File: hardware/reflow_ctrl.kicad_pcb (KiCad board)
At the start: 2 copper layers, 22 parts, among them IC1 MAX6675, U2 MOC3063, U3 BTA41/600B, X1 Master, X2 Mains, X3 Load, X4 Thermocouple

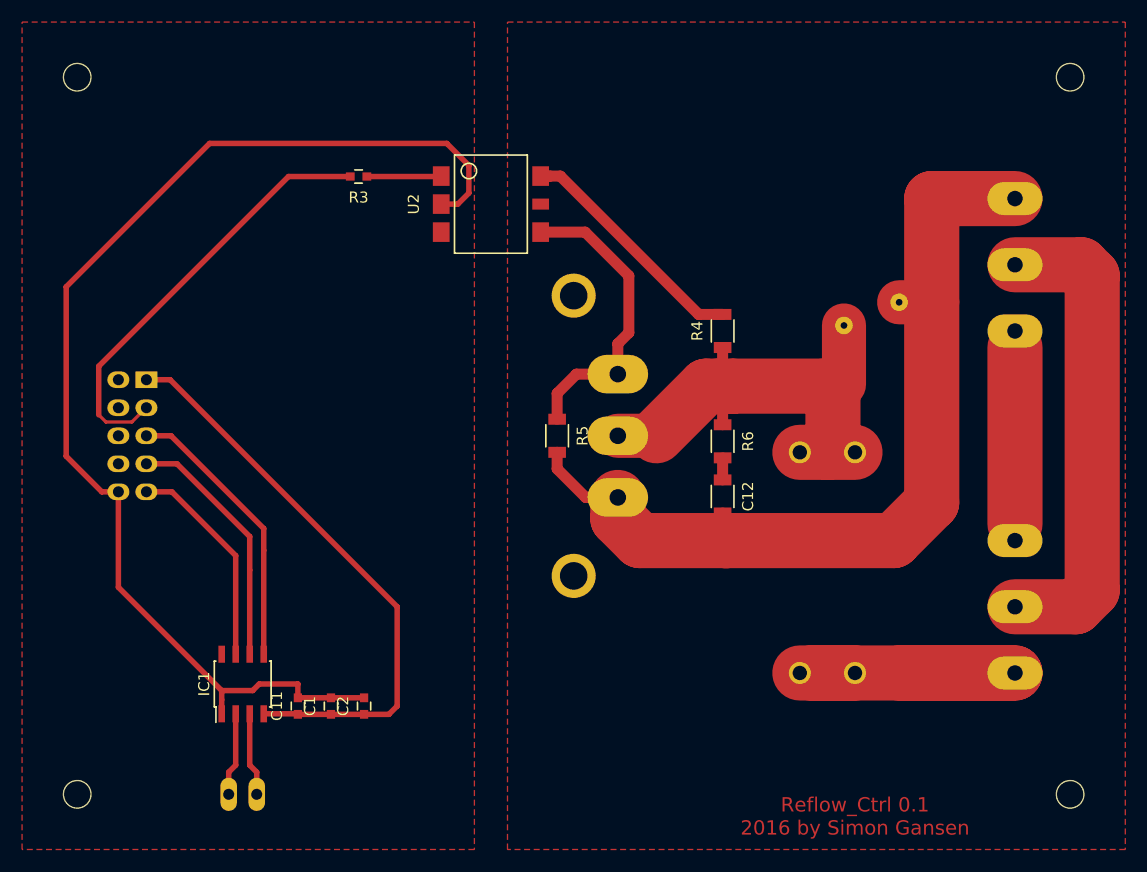
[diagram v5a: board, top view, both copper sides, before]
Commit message: Optimize header pinout and trace widths
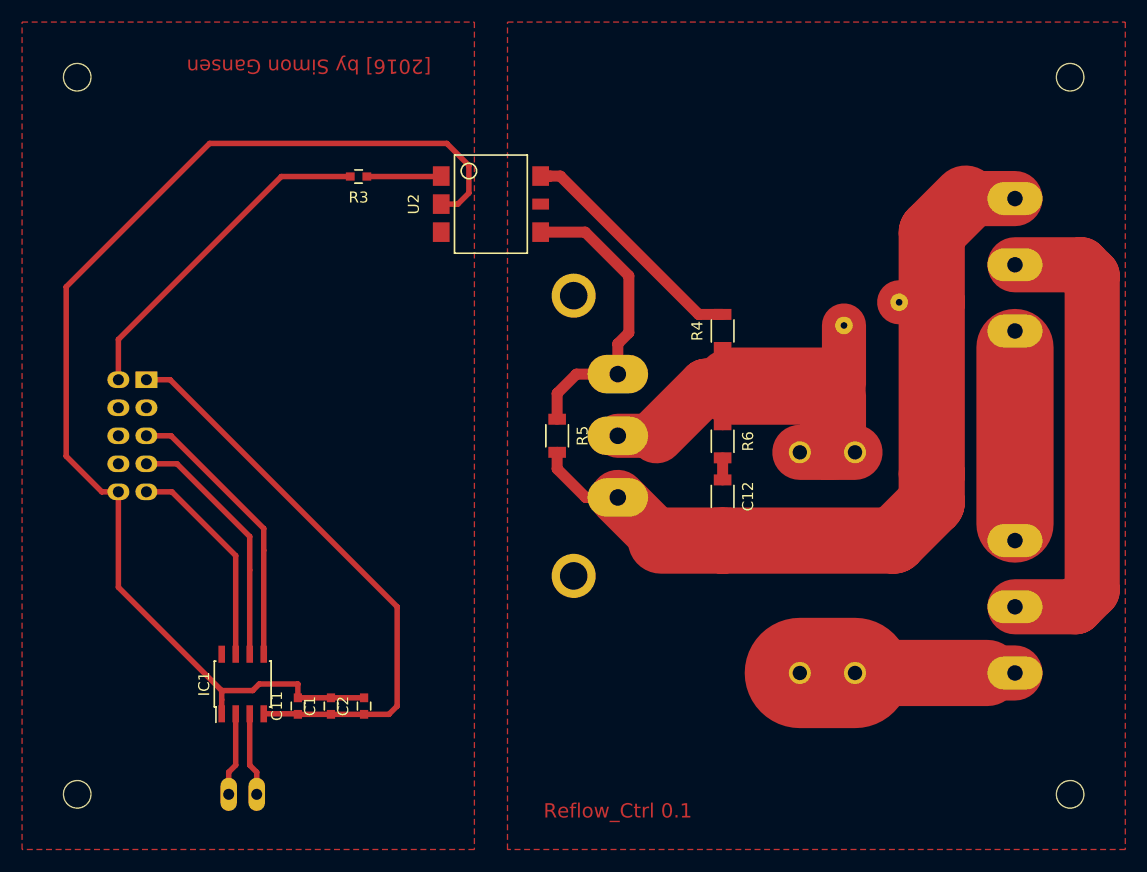
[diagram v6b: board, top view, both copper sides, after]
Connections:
- HS1 pad 1: (no net) -> /PE_mains
- X1 pad 2: (no net) -> /PWR
- X1 pad 3: /PWR -> (no net)
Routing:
- net /L_mains: track 34.0 -> 19.5 mm
- net /PWR: track 39.4 -> 30.8 mm
- net /L_load: track 84.8 -> 81.5 mm
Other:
- rule trace_min: 0.2 -> 0.3
- board text added: "Reflow_Ctrl 0.1"
- board text added: "[2016] by Simon Gansen"
- board text removed: "Reflow_Ctrl 0.1 2016 by Simon Gansen"
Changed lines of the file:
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@@
 (kicad_pcb (version 4) (host pcbnew "(2015-09-12 BZR 6188)-product")
   (general
-    (links 33)
+    (links 35)
     (no_connects 0)
-    (area 0 0 0 0)
+    (area 95.615476 49.075 213 132.700001)
     (thickness 1.6)
-    (drawings 9)
-    (tracks 113)
+    (drawings 10)
+    (tracks 110)
     (zones 0)
     (modules 22)
@@
     (zone_clearance 1)
     (zone_45_only no)
-    (trace_min 0.2)
+    (trace_min 0.3)
     (segment_width 0.15)
     (edge_width 0.15)
@@
     (pad 1 thru_hole rect (at -5.08 -1.27 270) (size 1.50622 2) (drill 0.99822) (layers *.Cu *.Mask)
       (net 2 +3V3))
-    (pad 2 thru_hole oval (at -5.08 1.27 270) (size 1.50622 2) (drill 0.99822) (layers *.Cu *.Mask))
-    (pad 3 thru_hole oval (at -2.54 -1.27 270) (size 1.50622 2) (drill 0.99822) (layers *.Cu *.Mask)
+    (pad 2 thru_hole oval (at -5.08 1.27 270) (size 1.50622 2) (drill 0.99822) (layers *.Cu *.Mask)
       (net 13 /PWR))
+    (pad 3 thru_hole oval (at -2.54 -1.27 270) (size 1.50622 2) (drill 0.99822) (layers *.Cu *.Mask))
     (pad 4 thru_hole oval (at -2.54 1.27 270) (size 1.50622 2) (drill 0.99822) (layers *.Cu *.Mask))
     (pad 5 thru_hole oval (at 0 -1.27 270) (size 1.50622 2) (drill 0.99822) (layers *.Cu *.Mask)
@@
     (fp_line (start 1.6 -0.7) (end 1.6 -0.9) (layer B.SilkS) (width 0.15))
     (pad 1 thru_hole circle (at -12.7 0 90) (size 4 4) (drill 2.5) (layers *.Cu *.Mask)
-      (zone_connect 2))
+      (net 8 /PE_mains) (zone_connect 2))
     (pad 1 thru_hole circle (at 12.7 0 90) (size 4 4) (drill 2.5) (layers *.Cu *.Mask)
-      (zone_connect 2))
+      (net 8 /PE_mains) (zone_connect 2))
   )
   (module uMIDI:Semi-Optotriac_MOC3063-SMD (layer F.Cu)
@@
       (net 3 /L_load))
   )
-  (gr_text "Reflow_Ctrl 0.1\n2016 by Simon Gansen" (at 175.5 122) (layer F.Cu)
+  (gr_text "[2016] by Simon Gansen" (at 126 54 180) (layer F.Cu)
+    (effects (font (size 1.3 1.3) (thickness 0.3)))
+  )
+  (gr_text "Reflow_Ctrl 0.1" (at 154 121.5) (layer F.Cu)
     (effects (font (size 1.3 1.3) (thickness 0.3)))
   )
@@
   (segment (start 121.905 112.7) (end 124.95 112.7) (width 0.5) (layer F.Cu) (net 2) (status 30))
   (segment (start 124.95 112.7) (end 125 112.75) (width 0.5) (layer F.Cu) (net 2) (status 30))
-  (segment (start 182.454179 93.545821) (end 182.454179 75.374221) (width 5) (layer F.Cu) (net 3))
-  (segment (start 182.454179 75.374221) (end 182.454179 66) (width 5) (layer F.Cu) (net 3))
+  (segment (start 179 97) (end 182.454179 93.545821) (width 6) (layer F.Cu) (net 3))
+  (segment (start 182.454179 93.545821) (end 182.454179 90.956185) (width 6) (layer F.Cu) (net 3))
+  (segment (start 163.5 97) (end 179 97) (width 6) (layer F.Cu) (net 3))
+  (segment (start 163.5 97) (end 157.912 97) (width 6) (layer F.Cu) (net 3))
+  (segment (start 157.912 97) (end 154 93.088) (width 5) (layer F.Cu) (net 3))
+  (segment (start 182.454179 75.374221) (end 182.454179 90.956185) (width 6) (layer F.Cu) (net 3))
+  (segment (start 163.610505 97) (end 164 97) (width 5) (layer F.Cu) (net 3))
+  (segment (start 182.454179 75.374221) (end 182.454179 69.074775) (width 6) (layer F.Cu) (net 3))
+  (segment (start 182.454179 69.074775) (end 185.528954 66) (width 6) (layer F.Cu) (net 3))
+  (segment (start 185.528954 66) (end 190 66) (width 5) (layer F.Cu) (net 3))
   (segment (start 179.5 75.4) (end 182.4284 75.4) (width 4) (layer F.Cu) (net 3))
   (segment (start 182.4284 75.4) (end 182.454179 75.374221) (width 3) (layer F.Cu) (net 3))
@@
   (segment (start 164 96.5) (end 164 96) (width 1) (layer F.Cu) (net 3))
   (segment (start 163.5 97) (end 164 96.5) (width 1) (layer F.Cu) (net 3))
-  (segment (start 182.454179 66) (end 190 66) (width 5) (layer F.Cu) (net 3))
-  (segment (start 156 97) (end 164 97) (width 5) (layer F.Cu) (net 3))
-  (segment (start 164 97) (end 163.610505 97) (width 5) (layer F.Cu) (net 3))
-  (segment (start 163.610505 97) (end 179 97) (width 5) (layer F.Cu) (net 3))
-  (segment (start 154 93.088) (end 154 95) (width 5) (layer F.Cu) (net 3))
-  (segment (start 154 95) (end 156 97) (width 5) (layer F.Cu) (net 3))
-  (segment (start 179 97) (end 182.454179 93.545821) (width 5) (layer F.Cu) (net 3))
   (segment (start 154 93.088) (end 154.412 93.5) (width 3) (layer F.Cu) (net 3) (status 30))
-  (segment (start 190 109) (end 171.5 109) (width 5) (layer F.Cu) (net 4))
-  (segment (start 179.5 109) (end 190 109) (width 5) (layer F.Cu) (net 4) (status 30))
-  (segment (start 170.5 109) (end 175.5 109) (width 5) (layer F.Cu) (net 4) (status 30))
+  (segment (start 187.5 109) (end 175.5 109) (width 6) (layer F.Cu) (net 4))
+  (segment (start 190 109) (end 187.5 109) (width 5) (layer F.Cu) (net 4))
+  (segment (start 170.5 109) (end 175.5 109) (width 10) (layer F.Cu) (net 4) (status 30))
   (segment (start 118.73 120) (end 118.73 117.99251) (width 0.5) (layer F.Cu) (net 5) (status 10))
   (segment (start 118.73 117.99251) (end 119.365 117.35751) (width 0.5) (layer F.Cu) (net 5))
@@
   (segment (start 197 73) (end 196 72) (width 5) (layer F.Cu) (net 8))
   (segment (start 190 103) (end 195.5 103) (width 5) (layer F.Cu) (net 8) (status 10))
-  (segment (start 190 79.5) (end 190 95.5) (width 5) (layer F.Cu) (net 9))
+  (segment (start 190 79.5) (end 190 95.5) (width 7) (layer F.Cu) (net 9))
   (segment (start 190 78) (end 190 79.5) (width 1) (layer F.Cu) (net 9))
   (segment (start 190 97) (end 190 95.5) (width 1) (layer F.Cu) (net 9))
@@
   (segment (start 119.365 98.365) (end 113.58 92.58) (width 0.5) (layer F.Cu) (net 12))
   (segment (start 113.58 92.58) (end 111.27 92.58) (width 0.5) (layer F.Cu) (net 12))
-  (segment (start 124.15 64) (end 129.75 64) (width 0.5) (layer F.Cu) (net 13))
-  (segment (start 109.95 86.25) (end 111.24 84.96) (width 0.3) (layer F.Cu) (net 13) (status 10))
-  (segment (start 109.95 86.25) (end 107.6 86.25) (width 0.3) (layer F.Cu) (net 13))
-  (segment (start 107.6 86.25) (end 106.95 85.6) (width 0.3) (layer F.Cu) (net 13))
-  (segment (start 106.95 81.2) (end 124.15 64) (width 0.5) (layer F.Cu) (net 13))
-  (segment (start 106.95 85.6) (end 106.95 81.2) (width 0.5) (layer F.Cu) (net 13))
-  (segment (start 111.27 84.96) (end 111.24 84.96) (width 0.3) (layer F.Cu) (net 13) (status 30))
+  (segment (start 108.73 78.77) (end 123.5 64) (width 0.5) (layer F.Cu) (net 13))
+  (segment (start 123.5 64) (end 129.75 64) (width 0.5) (layer F.Cu) (net 13))
+  (segment (start 108.73 82.42) (end 108.73 78.77) (width 0.5) (layer F.Cu) (net 13))
   (segment (start 163.5 89.5) (end 163.5 91.5) (width 1) (layer F.Cu) (net 14) (status 30))
   (segment (start 163.5 76.5) (end 161.328441 76.5) (width 1) (layer F.Cu) (net 15))
@@
   (segment (start 162 83) (end 163 83) (width 5) (layer F.Cu) (net 17))
   (segment (start 163 83) (end 164.436256 83) (width 5) (layer F.Cu) (net 17))
-  (segment (start 164.436256 83) (end 172.650147 83) (width 5) (layer F.Cu) (net 17))
+  (segment (start 164.436256 83) (end 172.650147 83) (width 7) (layer F.Cu) (net 17))
   (segment (start 172.650147 83) (end 173.5 83.849853) (width 5) (layer F.Cu) (net 17))
   (segment (start 157.5 87.5) (end 162 83) (width 5) (layer F.Cu) (net 17))
   (segment (start 154 87.5) (end 157.5 87.5) (width 4) (layer F.Cu) (net 17))
-  (segment (start 173.5 83.849853) (end 173.5 88.505825) (width 5) (layer F.Cu) (net 17))
+  (segment (start 173.5 83.849853) (end 173.5 88.505825) (width 6) (layer F.Cu) (net 17))
   (segment (start 175.5 89) (end 173.005825 89) (width 5) (layer F.Cu) (net 17))
   (segment (start 173.005825 89) (end 170.5 89) (width 5) (layer F.Cu) (net 17))

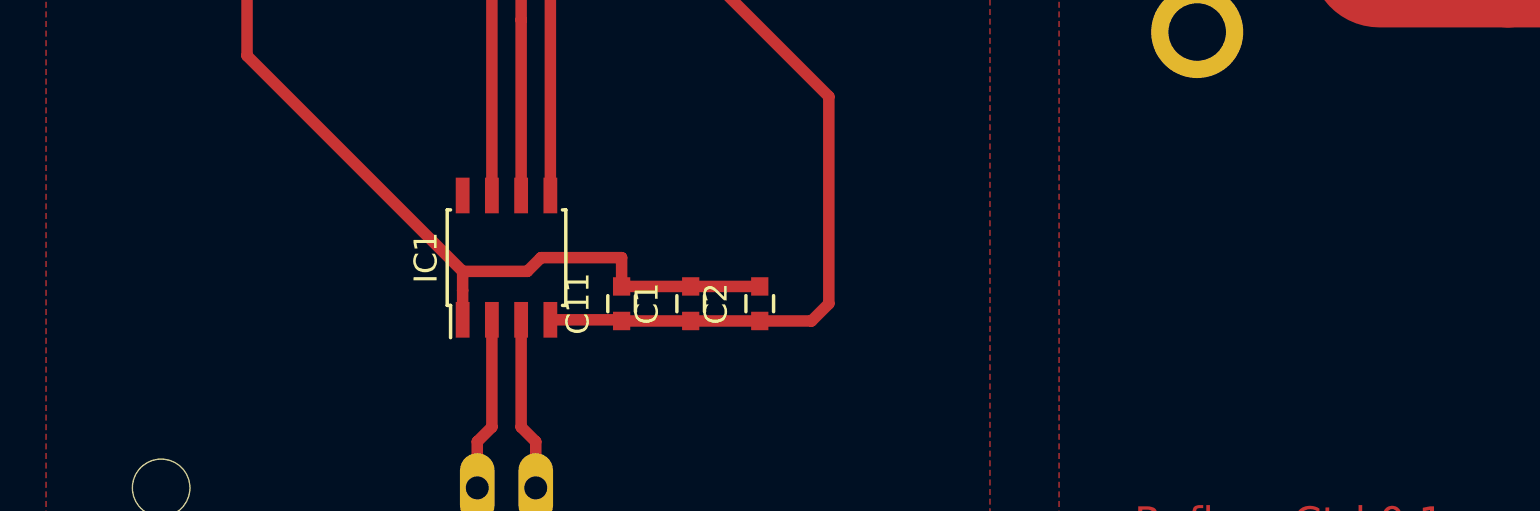
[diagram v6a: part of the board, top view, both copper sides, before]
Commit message: Add some fancy symbols
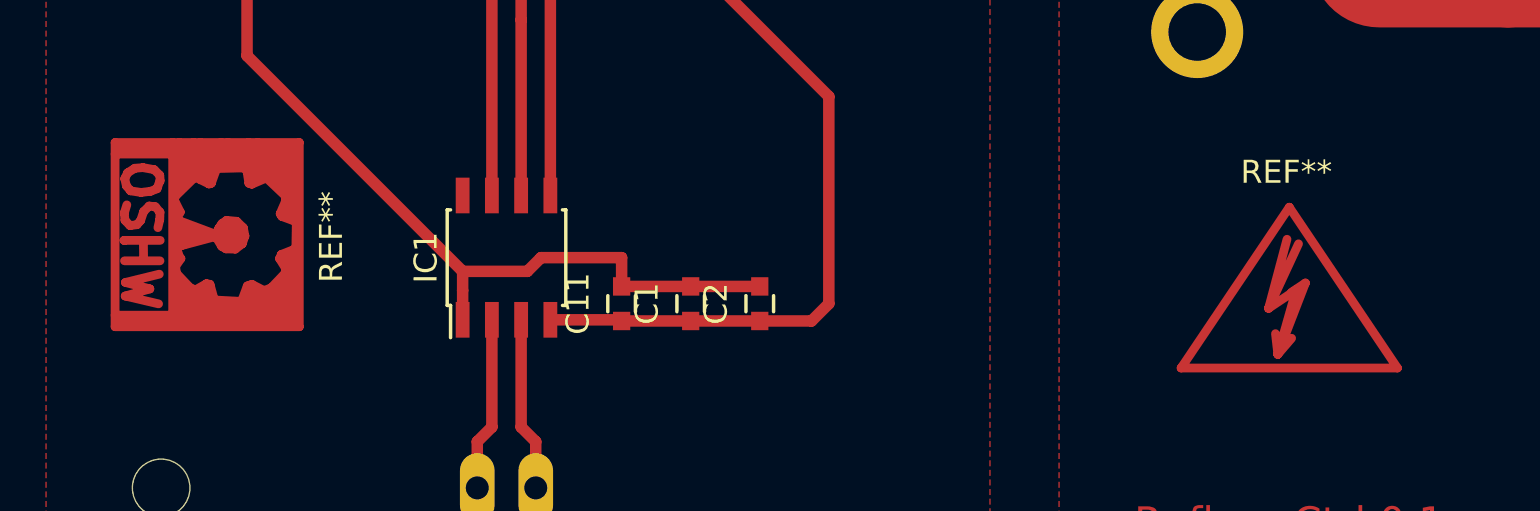
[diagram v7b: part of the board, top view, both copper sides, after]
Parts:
- added REF**: Symbol_HighVoltage_Type2_CopperTop_VerySmall, Symbols:Symbol_HighVoltage_Type2_CopperTop_VerySmall, F.Cu at (154.0, 112.0)
- added REF**: Symbol_OSHW-Logo_CopperTop_Negative, Symbols:Symbol_OSHW-Logo_CopperTop_Negative, F.Cu at (108.0, 109.0)

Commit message: Fix missing GND on TC-
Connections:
- HS1 pad 1: /PE_mains -> (no net)
- IC1 pad 2: /TC- -> GND
- IC1 pad 8: (no net) -> Net-(IC1-Pad8)
- X1 pad 3: (no net) -> Net-(X1-Pad3)
- X1 pad 4: (no net) -> Net-(X1-Pad4)
- X1 pad 6: (no net) -> Net-(X1-Pad6)
- X1 pad 8: (no net) -> Net-(X1-Pad8)
- X4 pad 2: /TC- -> GND
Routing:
- net GND: track 108.0 -> 115.5 mm
- net /TC-: track 7.56 -> 0.00 mm
